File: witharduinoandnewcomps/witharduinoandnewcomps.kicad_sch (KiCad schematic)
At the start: 20 parts, among them J1 FH34SRJ-24S-0.5SH_99_, Q2 ZXM61N03F, Q3 ZXM61N03F, SW1 Button-THT - 2-1825910-7

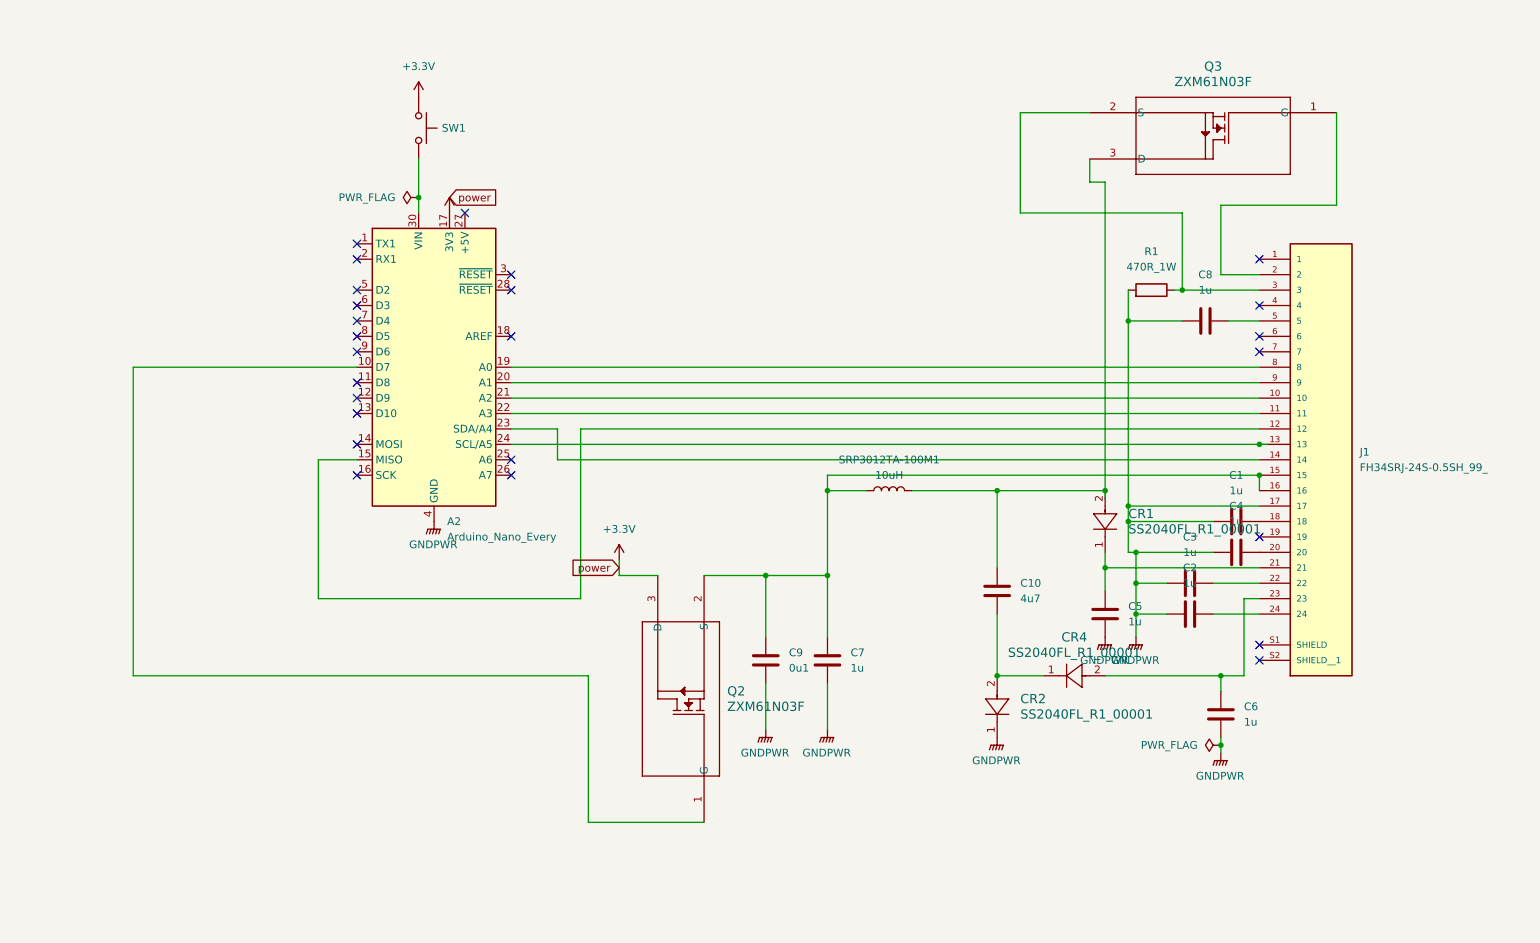
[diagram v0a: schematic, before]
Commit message: nov 8th changed back to raspberry pico
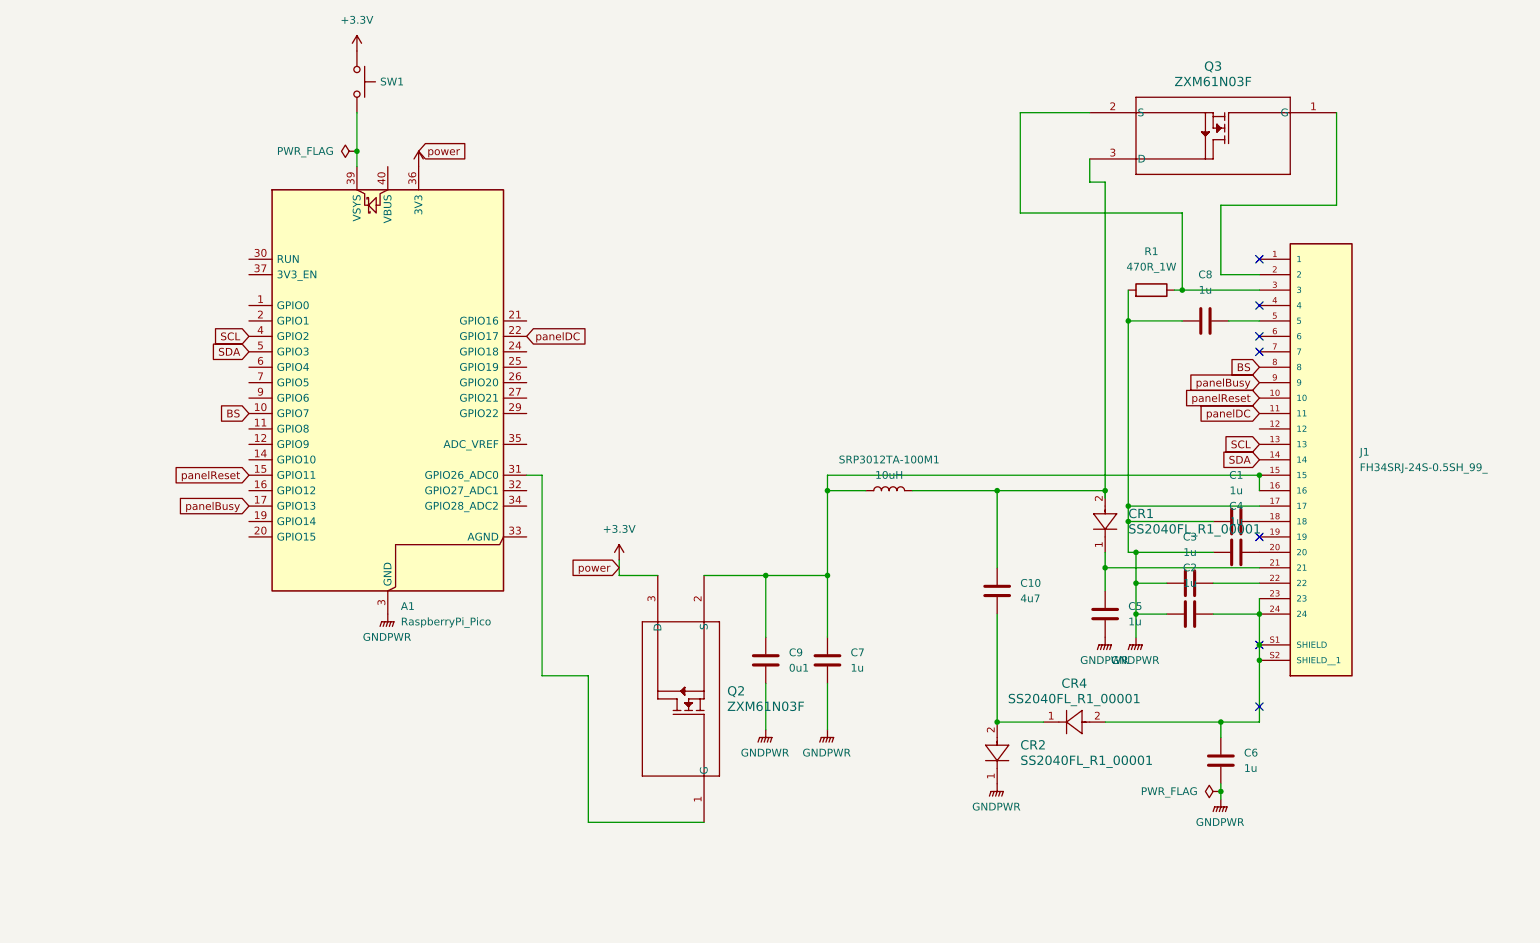
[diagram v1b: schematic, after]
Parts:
- removed A2: Arduino_Nano_Every, Module:Arduino_Nano, symbol MCU_Module:Arduino_Nano_Every
- added A1: RaspberryPi_Pico, Module:RaspberryPi_Pico_Common_Unspecified, symbol MCU_Module:RaspberryPi_Pico
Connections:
- net +3.3V: now also A1.36 (3V3)
- net GNDPWR: now also A1.13 (GND), A1.18 (GND), A1.23 (GND), A1.28 (GND), A1.3 (GND), A1.38 (GND), A1.8 (GND)
- net panelReset: now reaches J1.10
- net panelReset: now also A1.15 (GPIO11)
- net panelDC: now reaches J1.11
- net panelDC: now also A1.22 (GPIO17)
- net SCL: now reaches J1.13
- net SCL: now also A1.4 (GPIO2)
- net SDA: now reaches J1.14
- net SDA: now also A1.5 (GPIO3)
- net at C6.2, CR4.2, J1.23: now also C2.2, J1.24, J1.S1 (SHIELD), J1.S2 (SHIELD__1)
- net BS: now reaches J1.8
- net BS: now also A1.10 (GPIO7)
- net panelBusy: now reaches J1.9
- net panelBusy: now also A1.17 (GPIO13)
- net at Q2.1 (G): now also A1.31 (GPIO26_ADC0)
- net at SW1.2: now also A1.39 (VSYS)
- no-connect marks 25 -> 7
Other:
- moved on the sheet: C6, CR2, CR4, SW1

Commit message: added new stuff:slow start
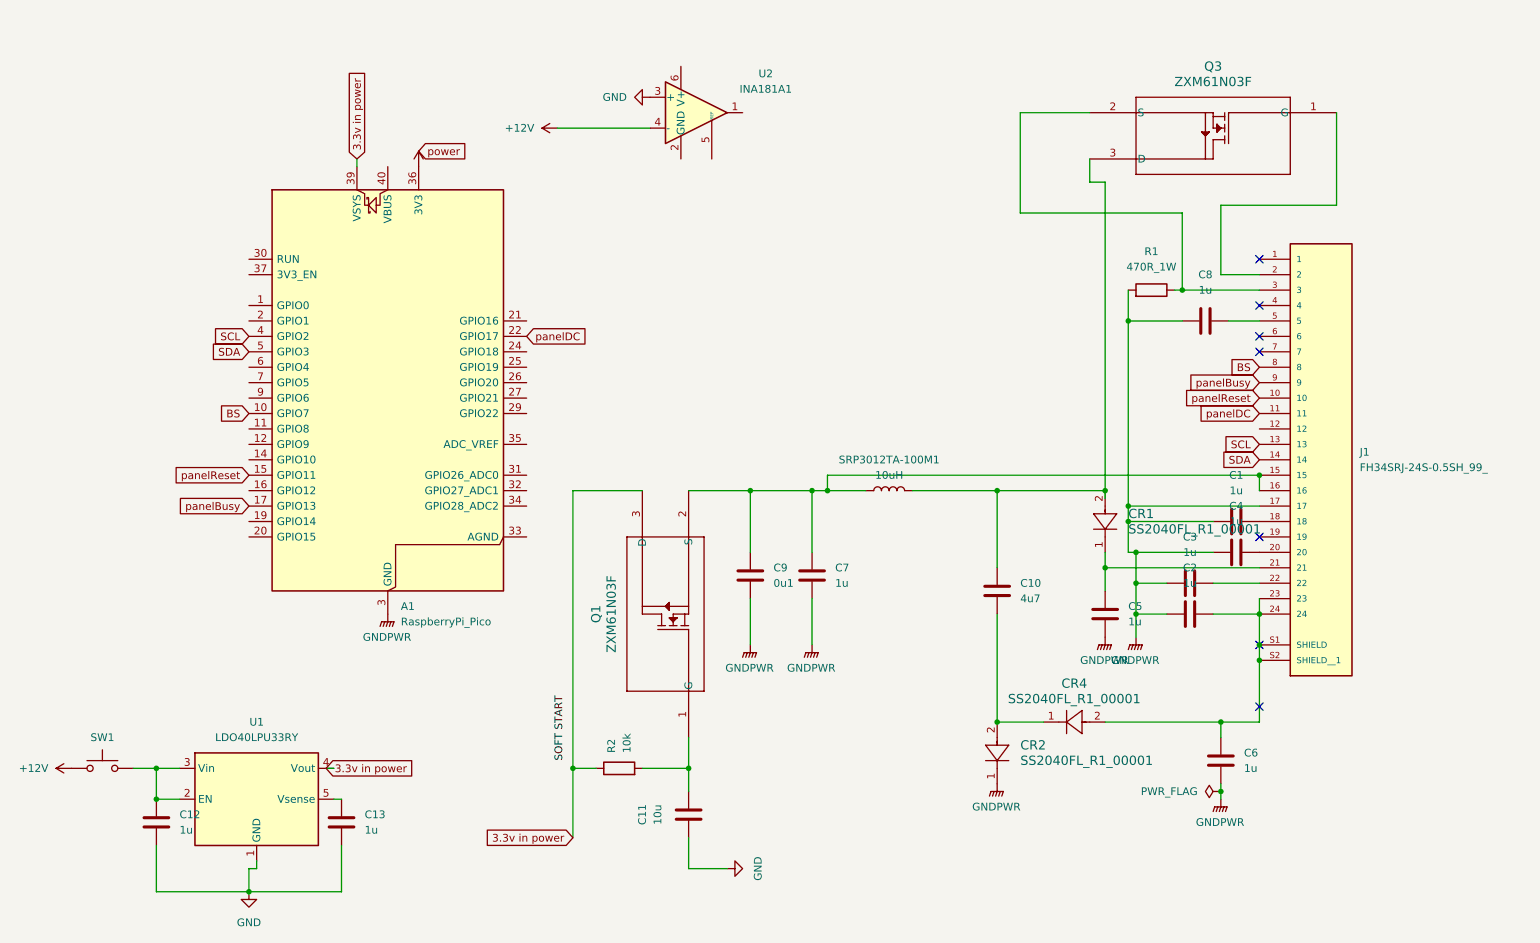
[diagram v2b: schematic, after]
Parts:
- removed Q2: ZXM61N03F, rsx_packages_TO_SOT:SOT-23, symbol rsx_Transistors:ZXM61N03F
- added C11: 10u, rsx_capacitors:C_0805_2012Metric, symbol rsx_Capacitors:10u
- added C12, C13: 1u, rsx_capacitors:C_0805_2012Metric, symbol rsx_Capacitors:1u
- added Q1: ZXM61N03F, rsx_packages_TO_SOT:SOT-23, symbol rsx_Transistors:ZXM61N03F
- added R2: 10k, rsx_resistors:R_0603_1608Metric, symbol rsx_Resistors:10k
- added U1: LDO40LPU33RY, Package_DFN_QFN:DFN-6-1EP_3x3mm_P0.95mm_EP1.7x2.6mm, symbol Regulator_Linear:LDO40LPU33RY
- added U2: INA181A1, rsx_packages_TO_SOT:SOT-23-6_DL, symbol rsx_opamps:INA181A1
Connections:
- net +3.3V: no longer SW1.1
- net at C7.2, C9.1, J1.15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: now also Q1.2 (S)
- net at SW1.2: now also C12.1, U1.2 (EN), U1.3 (Vin); no longer A1.39 (VSYS)
- new net: C13.1, U1.5 (Vsense)
- new net: C11.2, Q1.1 (G), R2.2
- new net +12V: SW1.1, U2.4 (-)
- new net 3.3v in power: A1.39 (VSYS), Q1.3 (D), R2.1, U1.4 (Vout)
- new net GND: C11.1, C12.2, C13.2, U1.1 (GND), U1.7 (GND), U2.3 (+)
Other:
- moved on the sheet: C7, C9, SW1
